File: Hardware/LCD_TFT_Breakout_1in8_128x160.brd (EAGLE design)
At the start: 40.6 x 59.7 mm, 66 parts, among them J1 MICRO-SD_CARD_SOCKETTINY, Q1 220mA/50V/3.5Ω, U2 TXB0108DQSR, U3 3.3V

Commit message: Update version to v10
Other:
- board text added: "v10"
- board text removed: "v03"
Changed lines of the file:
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@@
 <?xml version="1.0" encoding="utf-8"?>
 <!DOCTYPE eagle SYSTEM "eagle.dtd">
-<eagle version="9.2.0">
+<eagle version="9.1.3">
 <drawing>
 <settings>
-<setting alwaysvectorfont="no"/>
+<setting alwaysvectorfont="yes"/>
 <setting verticaltext="up"/>
 </settings>
@@
 <layer number="44" name="Drills" color="7" fill="1" visible="no" active="yes"/>
 <layer number="45" name="Holes" color="7" fill="1" visible="yes" active="yes"/>
-<layer number="46" name="Milling" color="3" fill="1" visible="yes" active="yes"/>
+<layer number="46" name="Milling" color="3" fill="1" visible="no" active="yes"/>
 <layer number="47" name="Measures" color="7" fill="1" visible="no" active="yes"/>
 <layer number="48" name="Document" color="7" fill="1" visible="no" active="yes"/>
@@
  the panel without changing location. This is a break-away option
  for the user</text>
-<text x="0.381" y="5.461" size="1.4732" layer="16" font="vector" ratio="15" rot="SMR90">v03</text>
+<text x="0.508" y="4.953" size="1.4732" layer="16" font="vector" ratio="15" rot="SMR90">v10</text>
 <text x="27.94" y="-23.241" size="1.778" layer="51" font="vector" ratio="15">Owen Lyke</text>
 <wire x1="6.223" y1="17.399" x2="0.381" y2="17.399" width="0.2032" layer="21"/>
@@
 <element name="FRAME1" library="SparkFun-Aesthetics" package="CREATIVE_COMMONS" value="FRAME-LETTER" x="0" y="-23.114">
 <attribute name="DESIGNER" value="Owen Lyke" x="0" y="-23.114" size="1.778" layer="27" display="off"/>
-<attribute name="REV" value="v03" x="0" y="-23.114" size="1.778" layer="27" display="off"/>
+<attribute name="REV" value="v10" x="0" y="-23.114" size="1.778" layer="27" display="off"/>
 </element>
 <element name="U2" library="SparkFun-IC-Comms" package="UFDFN-20" value="TXB0108DQSR" x="23.114" y="8.636" rot="R180">

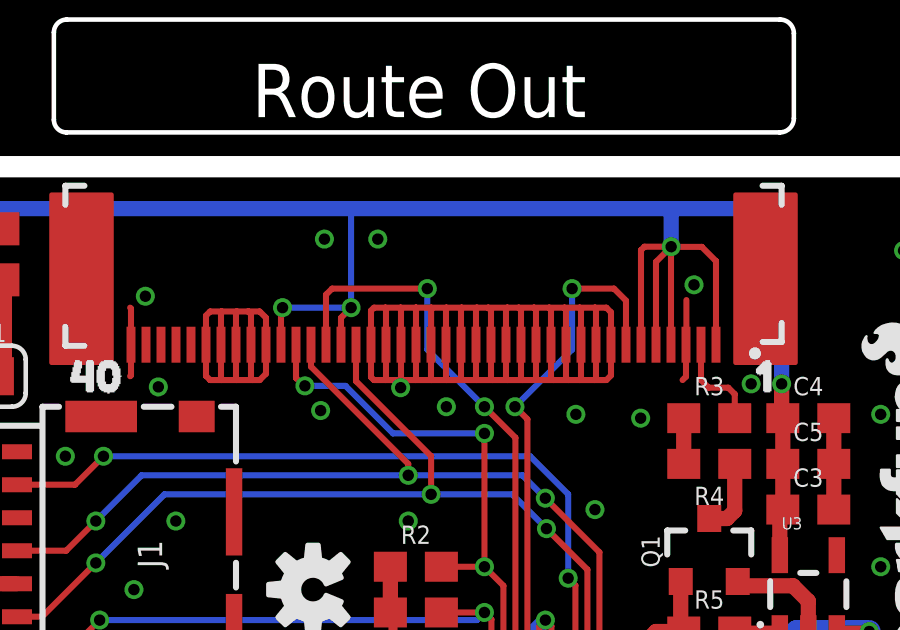
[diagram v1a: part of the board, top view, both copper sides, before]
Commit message: Remove wire stubs
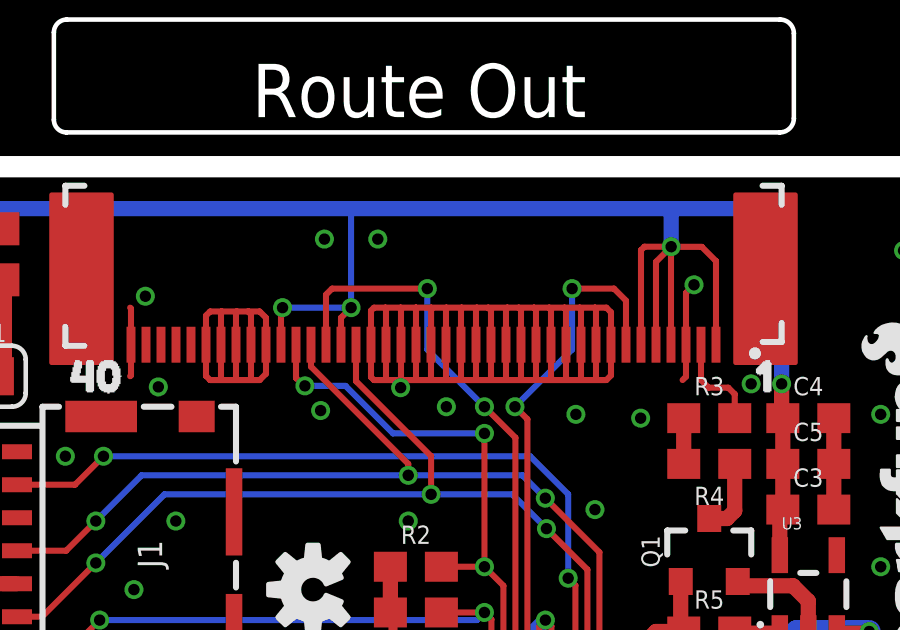
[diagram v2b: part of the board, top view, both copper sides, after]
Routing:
- net GND: track 94.0 -> 94.7 mm
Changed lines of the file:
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@@
 <layer number="23" name="tOrigins" color="15" fill="1" visible="yes" active="yes"/>
 <layer number="24" name="bOrigins" color="15" fill="1" visible="yes" active="yes"/>
-<layer number="25" name="tNames" color="7" fill="1" visible="no" active="yes"/>
-<layer number="26" name="bNames" color="7" fill="1" visible="no" active="yes"/>
-<layer number="27" name="tValues" color="7" fill="1" visible="no" active="yes"/>
-<layer number="28" name="bValues" color="7" fill="1" visible="no" active="yes"/>
-<layer number="29" name="tStop" color="7" fill="3" visible="no" active="yes"/>
-<layer number="30" name="bStop" color="7" fill="6" visible="no" active="yes"/>
-<layer number="31" name="tCream" color="7" fill="4" visible="no" active="yes"/>
-<layer number="32" name="bCream" color="7" fill="5" visible="no" active="yes"/>
-<layer number="33" name="tFinish" color="6" fill="3" visible="no" active="yes"/>
-<layer number="34" name="bFinish" color="6" fill="6" visible="no" active="yes"/>
-<layer number="35" name="tGlue" color="7" fill="4" visible="no" active="yes"/>
-<layer number="36" name="bGlue" color="7" fill="5" visible="no" active="yes"/>
-<layer number="37" name="tTest" color="7" fill="1" visible="no" active="yes"/>
-<layer number="38" name="bTest" color="7" fill="1" visible="no" active="yes"/>
-<layer number="39" name="tKeepout" color="4" fill="11" visible="no" active="yes"/>
-<layer number="40" name="bKeepout" color="1" fill="11" visible="no" active="yes"/>
-<layer number="41" name="tRestrict" color="4" fill="10" visible="no" active="yes"/>
-<layer number="42" name="bRestrict" color="1" fill="10" visible="no" active="yes"/>
-<layer number="43" name="vRestrict" color="2" fill="10" visible="no" active="yes"/>
-<layer number="44" name="Drills" color="7" fill="1" visible="no" active="yes"/>
+<layer number="25" name="tNames" color="7" fill="1" visible="yes" active="yes"/>
+<layer number="26" name="bNames" color="7" fill="1" visible="yes" active="yes"/>
+<layer number="27" name="tValues" color="7" fill="1" visible="yes" active="yes"/>
+<layer number="28" name="bValues" color="7" fill="1" visible="yes" active="yes"/>
+<layer number="29" name="tStop" color="7" fill="3" visible="yes" active="yes"/>
+<layer number="30" name="bStop" color="7" fill="6" visible="yes" active="yes"/>
+<layer number="31" name="tCream" color="7" fill="4" visible="yes" active="yes"/>
+<layer number="32" name="bCream" color="7" fill="5" visible="yes" active="yes"/>
+<layer number="33" name="tFinish" color="6" fill="3" visible="yes" active="yes"/>
+<layer number="34" name="bFinish" color="6" fill="6" visible="yes" active="yes"/>
+<layer number="35" name="tGlue" color="7" fill="4" visible="yes" active="yes"/>
+<layer number="36" name="bGlue" color="7" fill="5" visible="yes" active="yes"/>
+<layer number="37" name="tTest" color="7" fill="1" visible="yes" active="yes"/>
+<layer number="38" name="bTest" color="7" fill="1" visible="yes" active="yes"/>
+<layer number="39" name="tKeepout" color="4" fill="11" visible="yes" active="yes"/>
+<layer number="40" name="bKeepout" color="1" fill="11" visible="yes" active="yes"/>
+<layer number="41" name="tRestrict" color="4" fill="10" visible="yes" active="yes"/>
+<layer number="42" name="bRestrict" color="1" fill="10" visible="yes" active="yes"/>
+<layer number="43" name="vRestrict" color="2" fill="10" visible="yes" active="yes"/>
+<layer number="44" name="Drills" color="7" fill="1" visible="yes" active="yes"/>
 <layer number="45" name="Holes" color="7" fill="1" visible="yes" active="yes"/>
-<layer number="46" name="Milling" color="3" fill="1" visible="no" active="yes"/>
-<layer number="47" name="Measures" color="7" fill="1" visible="no" active="yes"/>
-<layer number="48" name="Document" color="7" fill="1" visible="no" active="yes"/>
-<layer number="49" name="Reference" color="7" fill="1" visible="no" active="yes"/>
-<layer number="50" name="dxf" color="7" fill="1" visible="no" active="yes"/>
+<layer number="46" name="Milling" color="3" fill="1" visible="yes" active="yes"/>
+<layer number="47" name="Measures" color="7" fill="1" visible="yes" active="yes"/>
+<layer number="48" name="Document" color="7" fill="1" visible="yes" active="yes"/>
+<layer number="49" name="Reference" color="7" fill="1" visible="yes" active="yes"/>
+<layer number="50" name="dxf" color="7" fill="1" visible="yes" active="yes"/>
 <layer number="51" name="tDocu" color="6" fill="1" visible="yes" active="yes"/>
-<layer number="52" name="bDocu" color="7" fill="1" visible="no" active="yes"/>
+<layer number="52" name="bDocu" color="7" fill="1" visible="yes" active="yes"/>
 <layer number="91" name="Nets" color="2" fill="1" visible="no" active="no"/>
 <layer number="92" name="Busses" color="1" fill="1" visible="no" active="no"/>
@@
 <layer number="95" name="Names" color="7" fill="1" visible="no" active="no"/>
 <layer number="96" name="Values" color="7" fill="1" visible="no" active="no"/>
-<layer number="2" name="Route2" color="16" fill="1" visible="no" active="yes"/>
-<layer number="15" name="Route15" color="23" fill="1" visible="no" active="yes"/>
+<layer number="2" name="Route2" color="16" fill="1" visible="yes" active="yes"/>
+<layer number="15" name="Route15" color="23" fill="1" visible="yes" active="yes"/>
 <layer number="53" name="tGND_GNDA" color="7" fill="9" visible="no" active="no"/>
 <layer number="54" name="bGND_GNDA" color="1" fill="9" visible="no" active="no"/>
@@
 <wire x1="9.3" y1="20.101" x2="9.3" y2="21.307" width="0.2032" layer="1"/>
 <wire x1="9.3" y1="21.307" x2="9.271" y2="21.336" width="0.2032" layer="1"/>
-<wire x1="11.8" y1="20.204" x2="11.8" y2="21.071" width="0.2032" layer="1"/>
 <wire x1="11.8" y1="21.071" x2="11.938" y2="21.209" width="0.2032" layer="1"/>
 <wire x1="11.938" y1="21.209" x2="12.319" y2="21.209" width="0.2032" layer="1"/>
@@
 <wire x1="13.208" y1="21.209" x2="13.589" y2="21.209" width="0.2032" layer="1"/>
 <wire x1="13.8" y1="20.998" x2="13.589" y2="21.209" width="0.2032" layer="1"/>
-<wire x1="12.3" y1="20.085" x2="12.3" y2="21.19" width="0.2032" layer="1"/>
 <wire x1="12.3" y1="21.19" x2="12.319" y2="21.209" width="0.2032" layer="1"/>
 <wire x1="9.3" y1="20.101" x2="9.3" y2="19.079" width="0.2032" layer="1"/>
@@
 <wire x1="22.914" y1="5.661" x2="22.987" y2="5.588" width="0.2032" layer="1"/>
 <via x="22.987" y="5.588" extent="1-16" drill="0.381"/>
-<wire x1="27.8" y1="20.101" x2="27.813" y2="20.088" width="0.2032" layer="1"/>
 <via x="2.032" y="24.765" extent="1-16" drill="0.381"/>
 <via x="1.143" y="18.669" extent="1-16" drill="0.381"/>
@@
 <wire x1="27.8" y1="19.037" x2="27.686" y2="18.923" width="0.2032" layer="1"/>
 <wire x1="27.8" y1="20.101" x2="27.813" y2="20.114" width="0.2032" layer="1"/>
-<wire x1="27.813" y1="20.114" x2="27.813" y2="21.59" width="0.2032" layer="1"/>
 <via x="29.972" y="18.796" extent="1-16" drill="0.381"/>
 <via x="28.067" y="22.098" extent="1-16" drill="0.381"/>
@@
 <via x="5.588" y="7.747" extent="1-16" drill="0.381"/>
 <via x="24.765" y="14.605" extent="1-16" drill="0.381"/>
+<wire x1="11.8" y1="20.101" x2="11.8" y2="21.071" width="0.2032" layer="1"/>
+<wire x1="12.3" y1="20.101" x2="12.3" y2="21.19" width="0.2032" layer="1"/>
+<wire x1="27.8" y1="20.101" x2="27.8" y2="21.831" width="0.2032" layer="1"/>
+<wire x1="27.8" y1="21.831" x2="28.067" y2="22.098" width="0.2032" layer="1"/>
 </signal>
 <signal name="SCLK">
